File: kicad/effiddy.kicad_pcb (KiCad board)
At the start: 2 copper layers, 135.6 x 119.7 mm, 62 parts

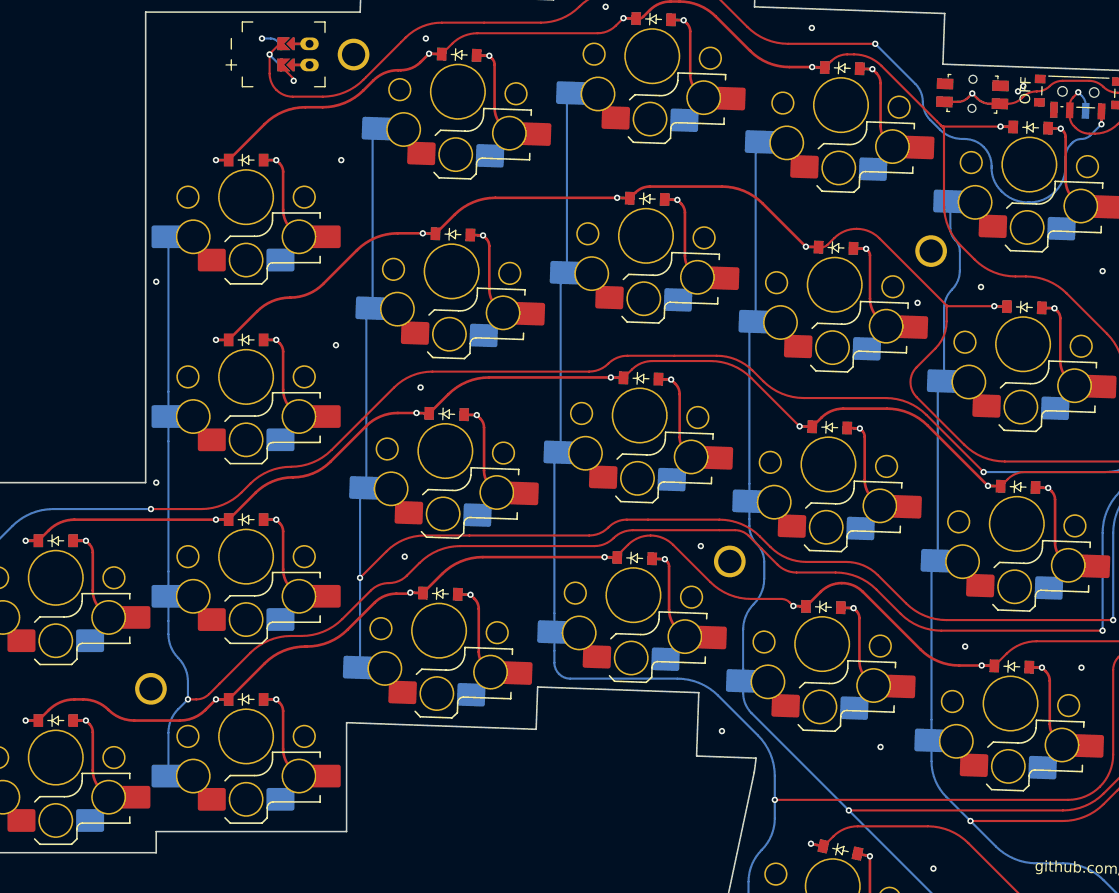
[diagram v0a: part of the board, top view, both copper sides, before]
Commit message: Updates pcb with 3d model, updates ergogen config
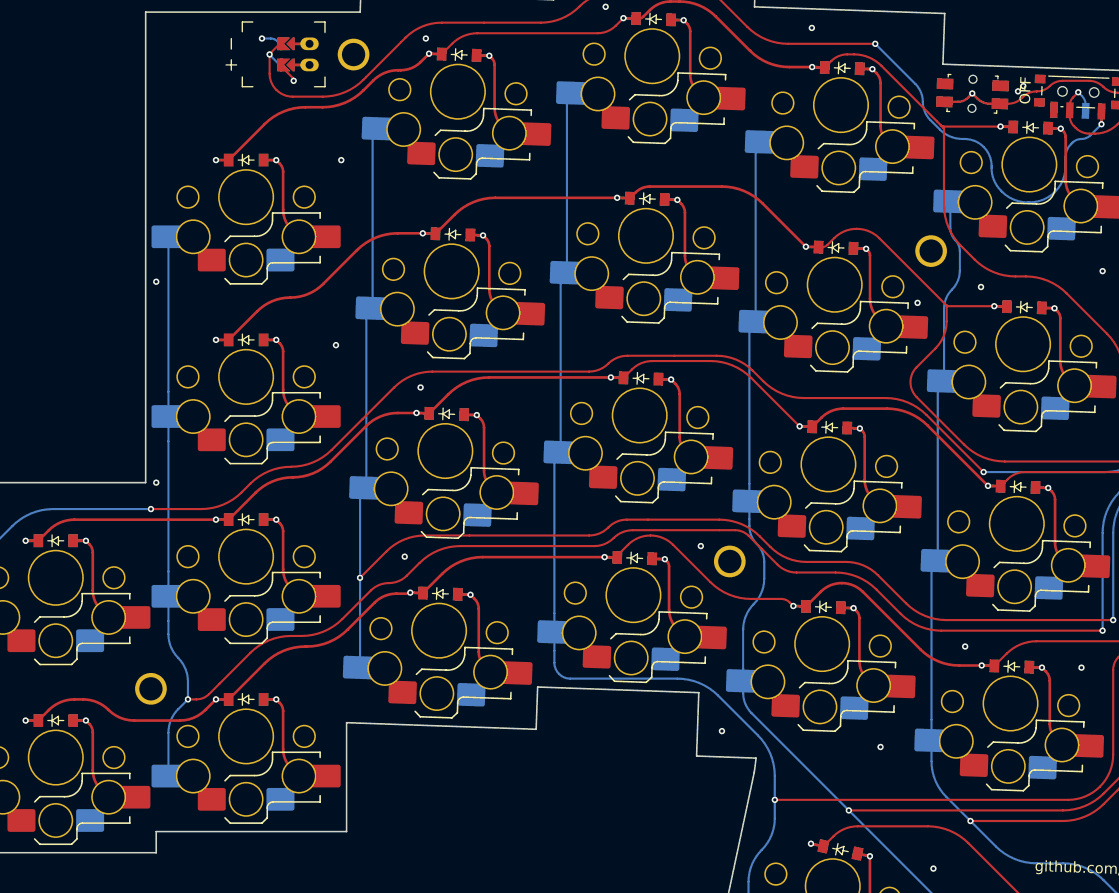
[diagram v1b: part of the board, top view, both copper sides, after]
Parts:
- D1, D10, D11, D12, D13, D14, D15, D16, D17, D18, D19, D2, D20, D21, D22, D23, D24, D25, D3, D4, D5, D6, D7, D8, D9: footprint ceoloide:diode_tht_sod123 -> Keyboard_Building:diode_tht_sod123
- JST1: footprint ceoloide:battery_connector_jst_ph_2 -> Keyboard_Building:battery_connector_jst_ph_2
- MCU1: footprint ceoloide:mcu_supermini_nrf52840 -> Keyboard_Building:mcu_supermini_nrf52840
- PWR1: footprint ceoloide:power_switch_smd_side -> Keyboard_Building:power_switch_smd_side
- RST1: footprint ceoloide:reset_switch_smd_side -> Keyboard_Building:reset_switch_smd_side
- S1, S10, S11, S12, S13, S14, S15, S16, S17, S18, S19, S2, S20, S21, S22, S23, S24, S25, S3, S4, S5, S6, S7, S8, S9: footprint ceoloide:switch_choc_v1_v2 -> Keyboard_Building:switch_choc_v1_v2
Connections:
- PWR1 pad 1: BAT_P -> (no net)
- PWR1 pad 3: BAT_P -> (no net)
- S1 pad : GND -> (no net)
- S10 pad : GND -> (no net)
- S11 pad : GND -> (no net)
- S12 pad : GND -> (no net)
- S13 pad : GND -> (no net)
- S14 pad : GND -> (no net)
- S15 pad : GND -> (no net)
- S16 pad : GND -> (no net)
- S17 pad : GND -> (no net)
- S18 pad : GND -> (no net)
- S19 pad : GND -> (no net)
- S2 pad : GND -> (no net)
- S20 pad : GND -> (no net)
- S21 pad : GND -> (no net)
- S22 pad : GND -> (no net)
- S23 pad : GND -> (no net)
- S24 pad : GND -> (no net)
- S25 pad : GND -> (no net)
- S3 pad : GND -> (no net)
- S4 pad : GND -> (no net)
- S5 pad : GND -> (no net)
- S6 pad : GND -> (no net)
- S7 pad : GND -> (no net)
- S8 pad : GND -> (no net)
- S9 pad : GND -> (no net)
